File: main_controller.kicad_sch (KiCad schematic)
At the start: 1 part, among them U2 RP2040

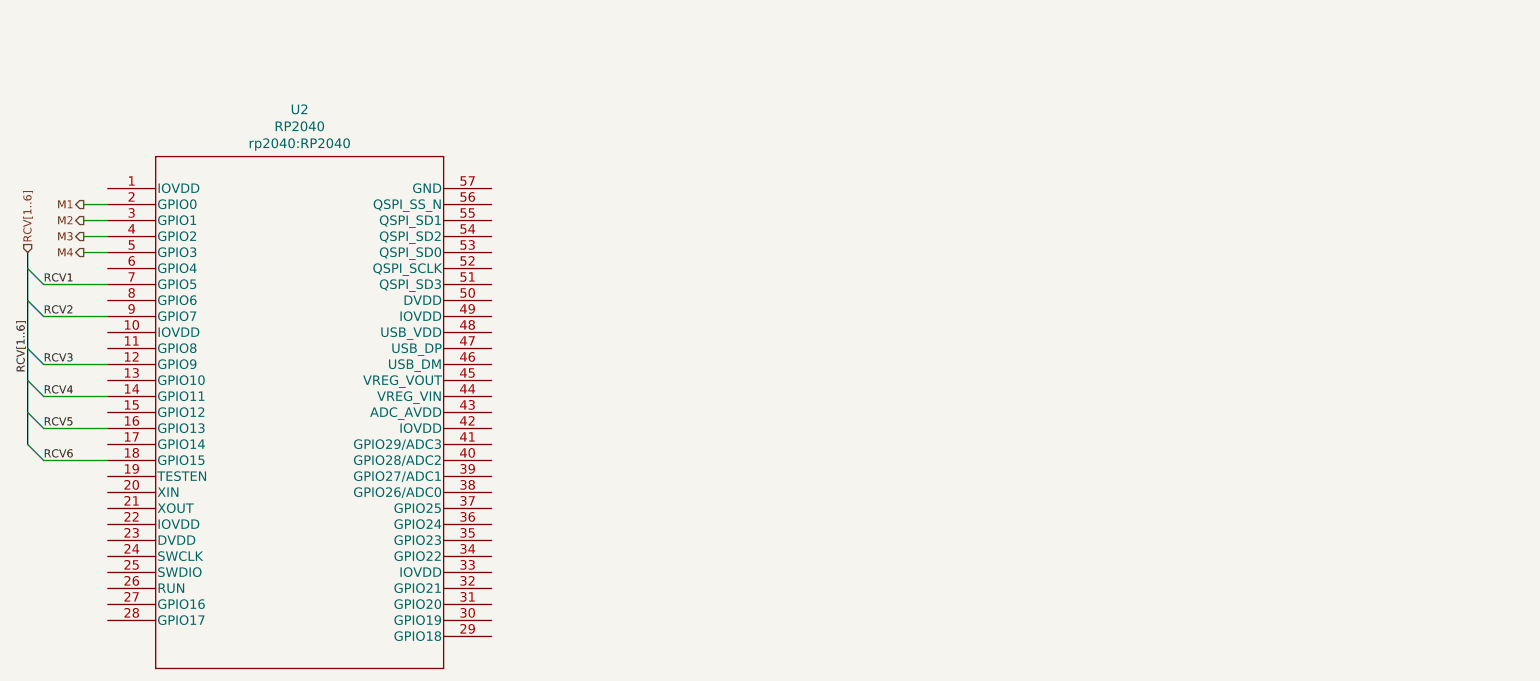
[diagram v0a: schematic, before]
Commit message: Add QSPI flash
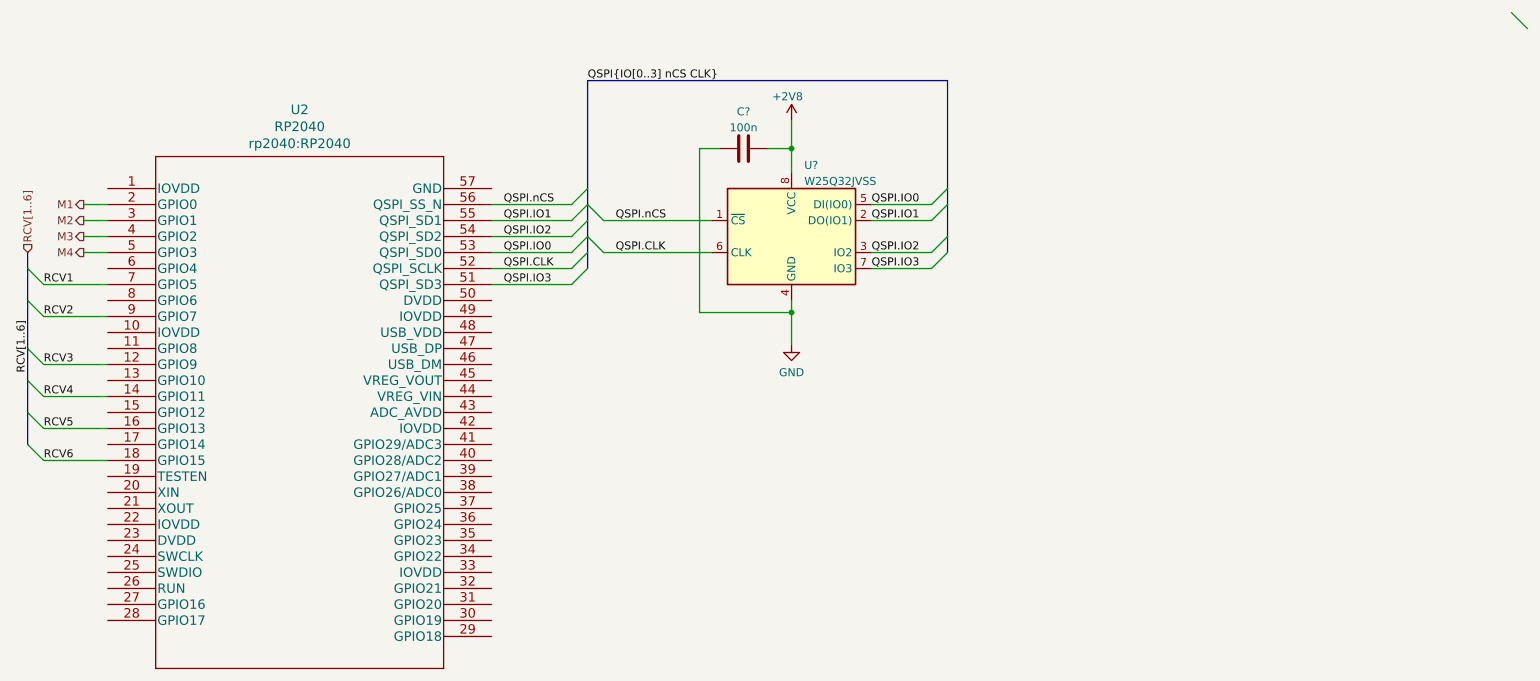
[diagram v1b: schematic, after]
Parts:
- added C?: 100n, symbol Device:C
- added U?: W25Q32JVSS, Package_SO:SOIC-8_5.23x5.23mm_P1.27mm, symbol Memory_Flash:W25Q32JVSS
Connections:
- net QSPI.IO3: now reaches U2.51 (QSPI_SD3)
- net QSPI.IO3: now also U?.7 (IO3)
- net QSPI.CLK: now reaches U2.52 (QSPI_SCLK)
- net QSPI.CLK: now also U?.6 (CLK)
- net QSPI.IO0: now reaches U2.53 (QSPI_SD0)
- net QSPI.IO0: now also U?.5 (DI(IO0))
- net QSPI.IO2: now reaches U2.54 (QSPI_SD2)
- net QSPI.IO2: now also U?.3 (IO2)
- net QSPI.IO1: now reaches U2.55 (QSPI_SD1)
- net QSPI.IO1: now also U?.2 (DO(IO1))
- net QSPI.nCS: now reaches U2.56 (QSPI_SS_N)
- net QSPI.nCS: now also U?.1 (~{CS})
- new net +2V8: C?.2, U?.8 (VCC)
- new net GND: C?.1, U?.4 (GND)
